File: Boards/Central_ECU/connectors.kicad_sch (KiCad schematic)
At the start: 44 parts, among them J10 Solenoid NANOFIT, J11 DB9 Microfit, J12 RS422 JST, J13 USB_B_Micro, J14 SWD JST PH, J15 UART JST, J2 Extras JST, J3 MICROFIT, J4 Siren MICROFIT, J5 I2CB JST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

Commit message: Updated resistors on ECU, added code to read battery voltages
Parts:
- R44: value 10K2 -> 18K
- R45: value 2K49 -> 2K7
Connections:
- net 4S_VOLTAGE renamed 6S_VOLTAGE
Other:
- note added: "6S"
- note added: "6S with max voltage 25.2V, nom 22.2V Allows 3S/4S (11.1V, max 12.6V / 16.8V, nom 14.8) And 7S (25.9, max 29.4V) Or regulated 24V input"
- note removed: "4S"
- note removed: "4S with max voltage 16.8V, nom 14.8. Also should allow for 3S (11.1V, max 12.6V) And 6-7S (22.2V, max 25.2 / 25.9, max 29.4V) Or regulated 24V input"
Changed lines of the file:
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@@
 		)
 	)
-	(text "4S with max voltage 16.8V, nom 14.8.\nAlso should allow for 3S (11.1V, max 12.6V)\nAnd 6-7S (22.2V, max 25.2 / 25.9, max 29.4V)\nOr regulated 24V input"
+	(text "6S with max voltage 25.2V, nom 22.2V\nAllows 3S/4S (11.1V, max 12.6V / 16.8V, nom 14.8)\nAnd 7S (25.9, max 29.4V)\nOr regulated 24V input"
 		(exclude_from_sim no)
 		(at 34.798 39.116 0)
@@
 		)
 	)
-	(text "4S"
+	(text "6S"
 		(exclude_from_sim no)
 		(at 48.006 53.848 0)
@@
 		)
 	)
-	(hierarchical_label "4S_VOLTAGE"
+	(hierarchical_label "6S_VOLTAGE"
 		(shape output)
 		(at 31.75 74.93 180)
@@
 			)
 		)
-		(property "Value" "2K49"
+		(property "Value" "2K7"
 			(at 132.08 80.0099 0)
 			(effects
@@
 			)
 		)
-		(property "Value" "10K2"
+		(property "Value" "18K"
 			(at 132.08 72.3899 0)
 			(effects

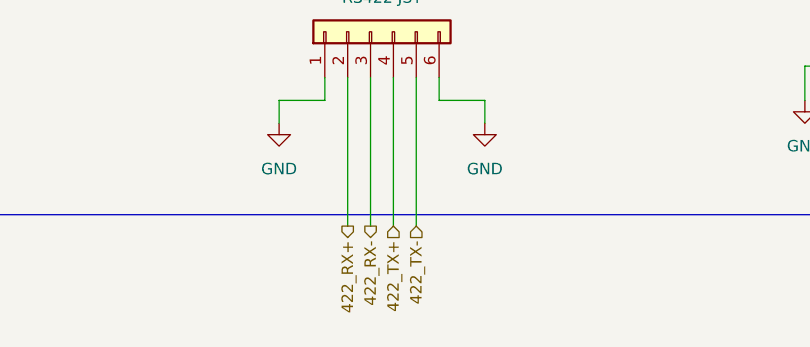
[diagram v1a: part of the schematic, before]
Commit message: Changes to reflect incorrect schematic labeling
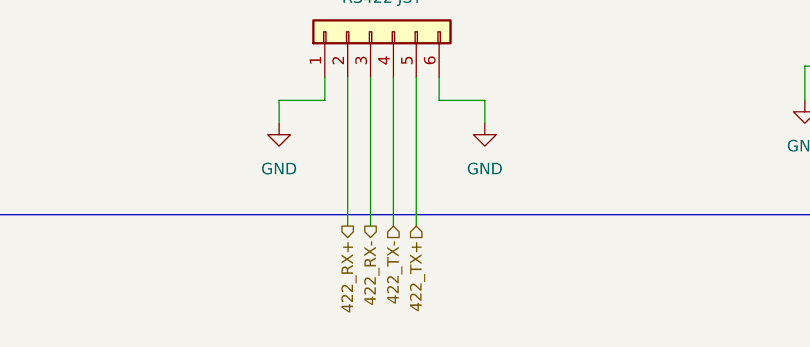
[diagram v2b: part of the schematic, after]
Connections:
- net 422_TX+: now also J12.5 (Pin_5); no longer J12.4 (Pin_4)
- net 422_TX-: now also J12.4 (Pin_4); no longer J12.5 (Pin_5)
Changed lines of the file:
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@@
 		)
 	)
-	(hierarchical_label "422_TX+"
+	(hierarchical_label "422_TX-"
 		(shape input)
 		(at 167.64 236.22 270)
@@
 		)
 	)
-	(hierarchical_label "422_TX-"
+	(hierarchical_label "422_TX+"
 		(shape input)
 		(at 170.18 236.22 270)
